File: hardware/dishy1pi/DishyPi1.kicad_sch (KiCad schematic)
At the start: 6 parts, among them J1 Conn_02x20_Odd_Even, U1 CAT24C256WI-GT3

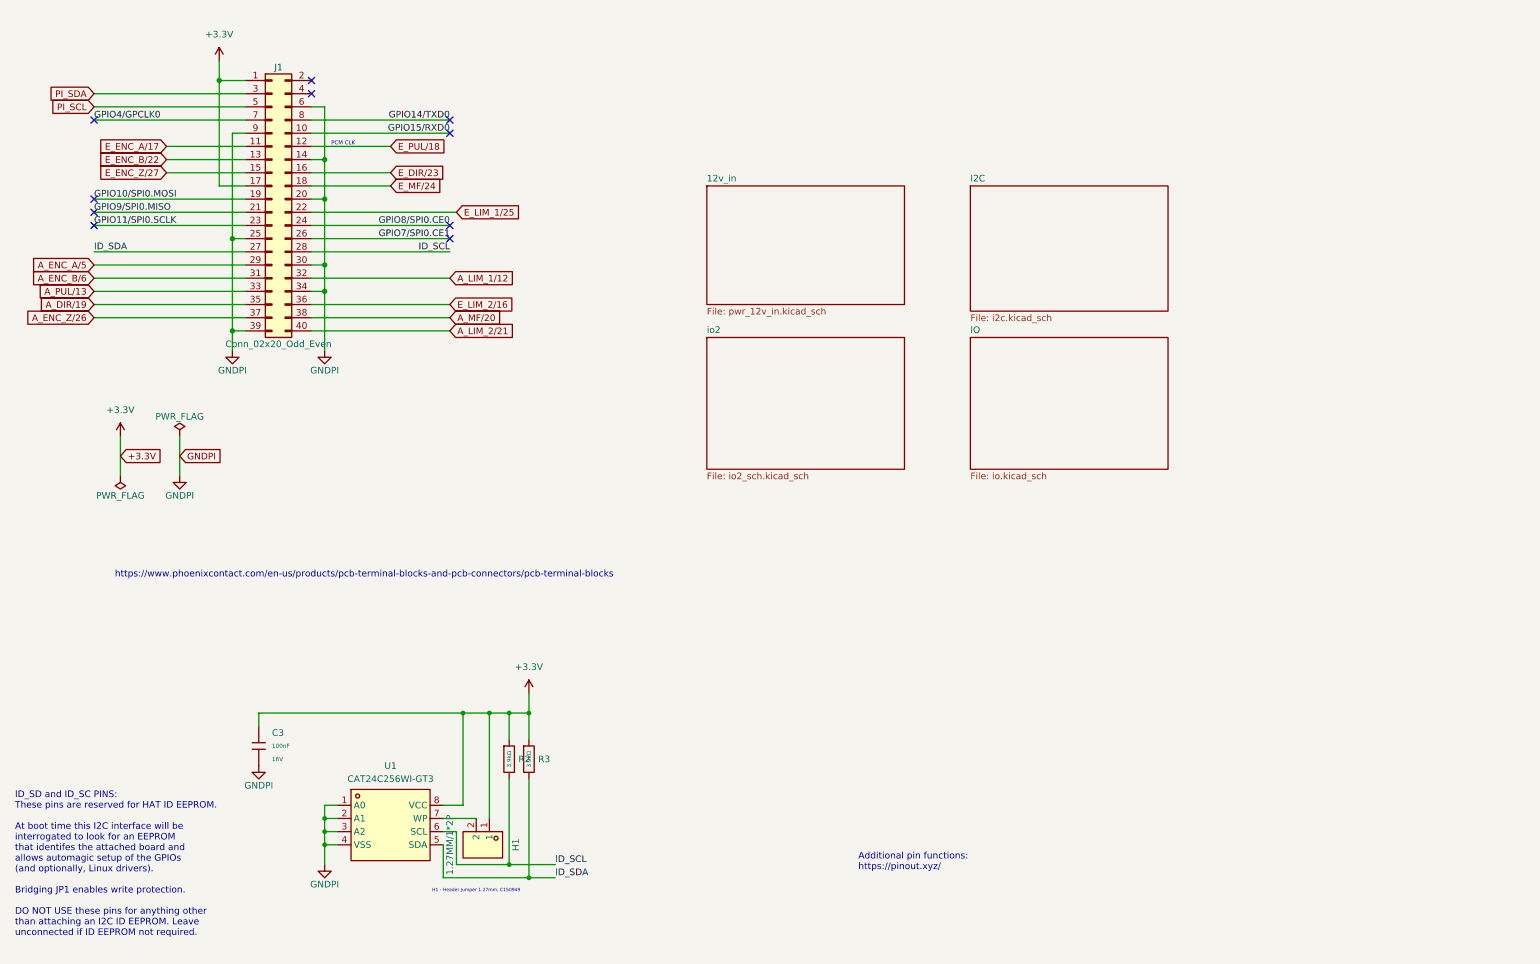
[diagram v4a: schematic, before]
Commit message: Added 12V power input
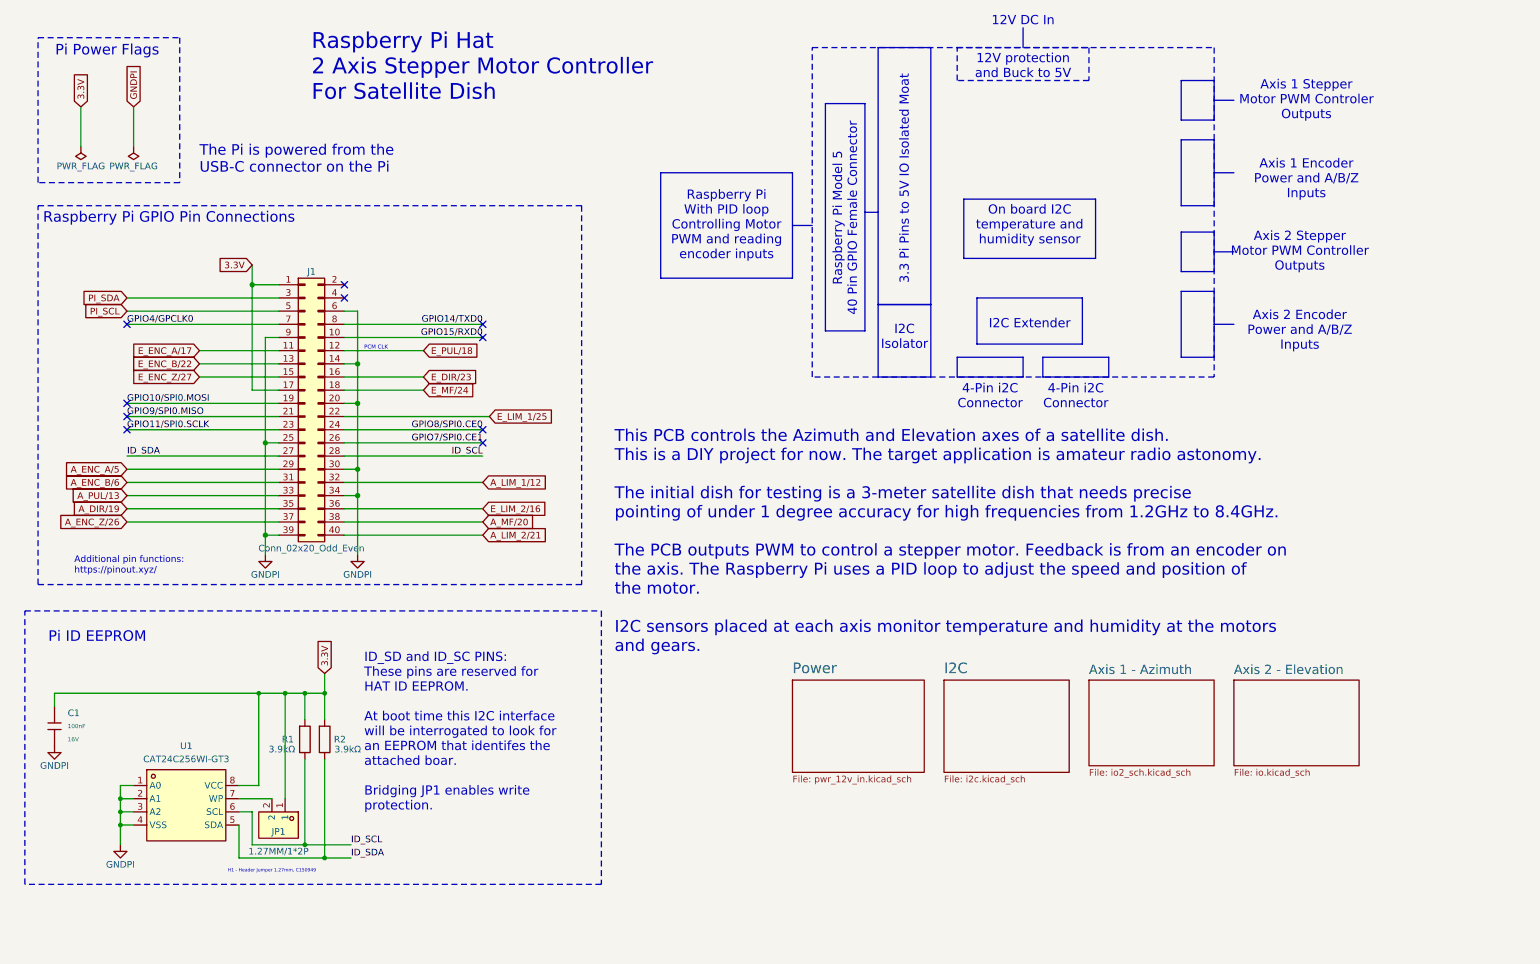
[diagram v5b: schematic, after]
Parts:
- renumbered C3 to C1, H1 to JP1, R2 to R1, R3 to R2
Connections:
- net +3.3V renamed 3.3V
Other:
- sheet 12v_in renamed Power
- sheet IO renamed Axis 2 - Elevation
- sheet io2 renamed Axis 1 - Azimuth
- note added: "12V DC In"
- note added: "3.3 Pi Pins to 5V IO Isolated Moat"
- note added: "4-Pin i2C Connector"
- note added: "Axis 1 Encoder Power and A/B/Z Inputs"
- note added: "Axis 1 Stepper Motor PWM Controler Outputs"
- note added: "Axis 2 Encoder Power and A/B/Z Inputs"
- note added: "Axis 2 Stepper Motor PWM Controller Outputs"
- note added: "I2C Extender"
- note added: "I2C Isolator"
- note added: "ID_SD and ID_SC PINS: These pins are reserved for HAT ID EEPROM. At boot time this I2C interface will be interrogated to look for an EEPROM that identifes the attached boar. Bridging JP1 enables write protection."
- note added: "On board I2C temperature and humidity sensor"
- note added: "Pi ID EEPROM"
- note added: "Pi Power Flags"
- note added: "Raspberry Pi Hat 2 Axis Stepper Motor Controller For Satellite Dish"
- note added: "Raspberry Pi Model 5 40 Pin GPIO Female Connector"
- note added: "Raspberry Pi With PID loop Controlling Motor PWM and reading encoder inputs"
- note added: "The Pi is powered from the USB-C connector on the Pi"
- note added: "This PCB controls the Azimuth and Elevation axes of a satellite dish. This is a DIY project for now. The target application is amateur radio astonomy. The initial dish for testing is a 3-meter satellite dish that needs precise pointing of under 1 degree accuracy for high frequencies from 1.2GHz to 8.4GHz. The PCB outputs PWM to control a stepper motor. Feedback is from an encoder on the axis. The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"
- note removed: "ID_SD and ID_SC PINS: These pins are reserved for HAT ID EEPROM. At boot time this I2C interface will be interrogated to look for an EEPROM that identifes the attached board and allows automagic setup of the GPIOs (and optionally, Linux drivers). Bridging JP1 enables write protection. DO NOT USE these pins for anything other than attaching an I2C ID EEPROM. Leave unconnected if ID EEPROM not requ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"
- note removed: "https://www.phoenixcontact.com/en-us/products/pcb-terminal-blocks-and-pcb-connectors/pcb-terminal-blocks"
- title: (none) -> Raspberry Pi Hat 2 Axis Stepper Motor Controller
- moved on the sheet: C1, J1, JP1, R1, R2, U1

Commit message: Pushed latest parts lib
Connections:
- net 5V_PI: now reaches J1.2 (Pin_2)
- net 5V_PI: now also J1.4 (Pin_4)
- net 3.3V renamed 3.3V_PI
- net A_DIR/19: no longer names the net of J1.35 (Pin_35)
- net A_ENC_A/5: no longer names the net of J1.29 (Pin_29)
- net A_ENC_B/6: no longer names the net of J1.31 (Pin_31)
- net A_ENC_Z/26: no longer names the net of J1.37 (Pin_37)
- net A_LIM_1/12: no longer names the net of J1.32 (Pin_32)
- net A_LIM_2/21: no longer names the net of J1.40 (Pin_40)
- net A_MF/20: no longer names the net of J1.38 (Pin_38)
- net A_PUL/13: no longer names the net of J1.33 (Pin_33)
- net E_DIR/23: no longer names the net of J1.16 (Pin_16)
- net E_ENC_A/17 renamed NRST_MCU
- net E_ENC_B/22 renamed BOOT0_MCU
- net E_ENC_Z/27: no longer names the net of J1.15 (Pin_15)
- net E_LIM_1/25: no longer names the net of J1.22 (Pin_22)
- net E_LIM_2/16: no longer names the net of J1.36 (Pin_36)
- net E_MF/24: no longer names the net of J1.18 (Pin_18)
- net E_PUL/18: no longer names the net of J1.12 (Pin_12)
- net GPIO10/SPI0.MOSI: no longer names the net of J1.19 (Pin_19)
- net GPIO11/SPI0.SCLK: no longer names the net of J1.23 (Pin_23)
- net GPIO14/TXD0 renamed UART_RX_MCU
- net GPIO15/RXD0 renamed UART_TX_MCU
- net GPIO4/GPCLK0: no longer names the net of J1.7 (Pin_7)
- net GPIO7/SPI0.CE1: no longer names the net of J1.26 (Pin_26)
- net GPIO8/SPI0.CE0: no longer names the net of J1.24 (Pin_24)
- net GPIO9/SPI0.MISO: no longer names the net of J1.21 (Pin_21)
- net PI_SCL renamed SCL_PI
- net PI_SDA renamed SDA_PI
- no-connect marks 10 -> 20
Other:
- added sheet MCU PID (mcu_pid.kicad_sch)
- note added: "5V_PI is used to convert to 3.3V for the PID MCU"
- note added: "Pi Pin 8 is Tx, 9 is Rx swapped into MCU Rx/Tx pins"
- note added: "Pin functions: https://pinout.xyz/"
- note added: "Raspberry Pi 40-Pin Header"
- note removed: "Additional pin functions: https://pinout.xyz/"
- note removed: "PCM CLK"
- moved on the sheet: J1
